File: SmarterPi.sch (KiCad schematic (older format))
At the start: 19 parts, among them J1 Raspberry_Pi_2_3, J2 RJ10, J3 Screw_Terminal_01x04, J4 Screw_Terminal_01x03, J5 Screw_Terminal_01x04, SW1 SW_Push, SW2 SW_Push, SW3 SW_Push

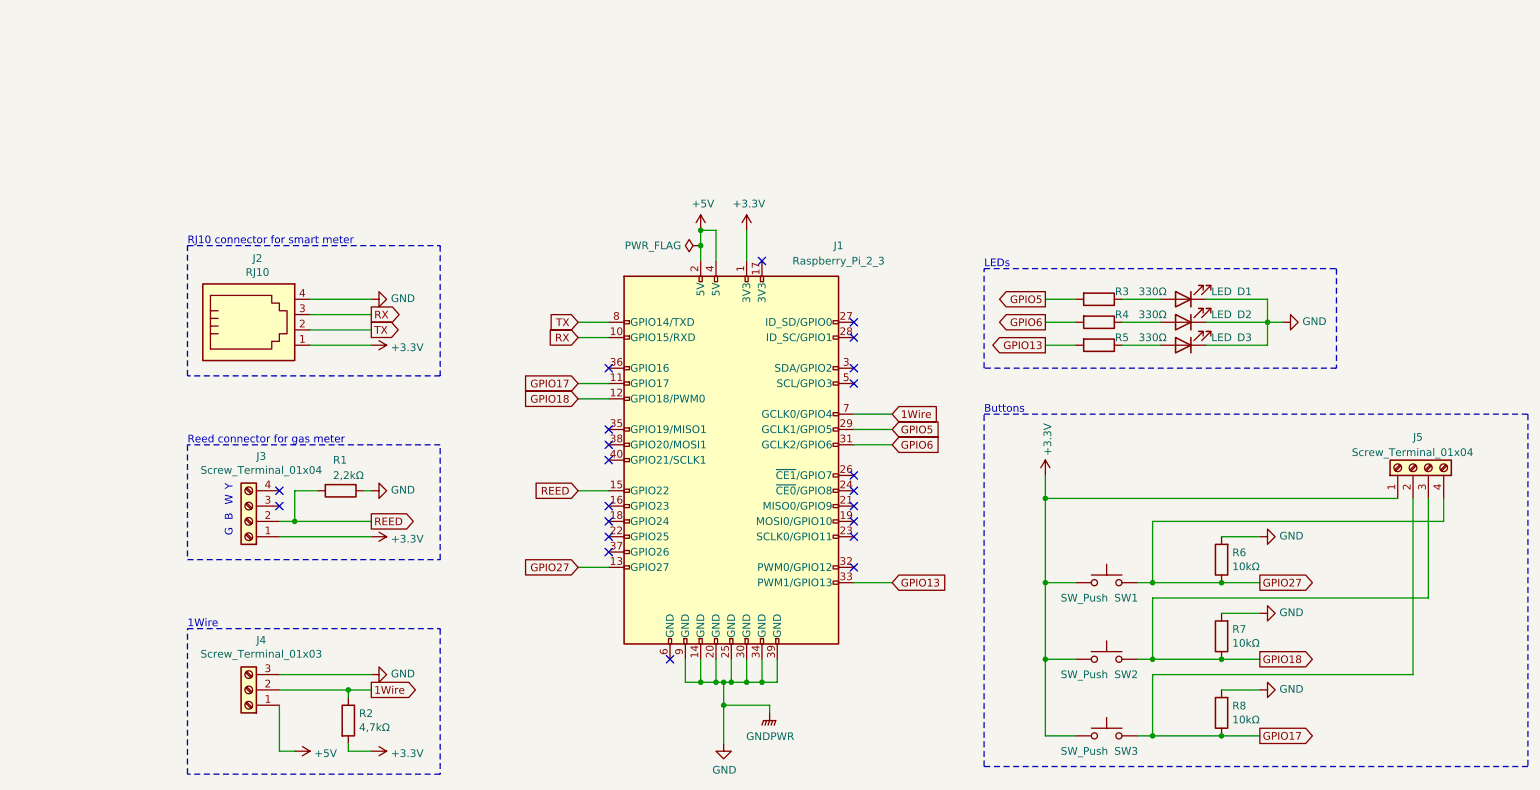
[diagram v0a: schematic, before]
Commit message: Added DS18B20
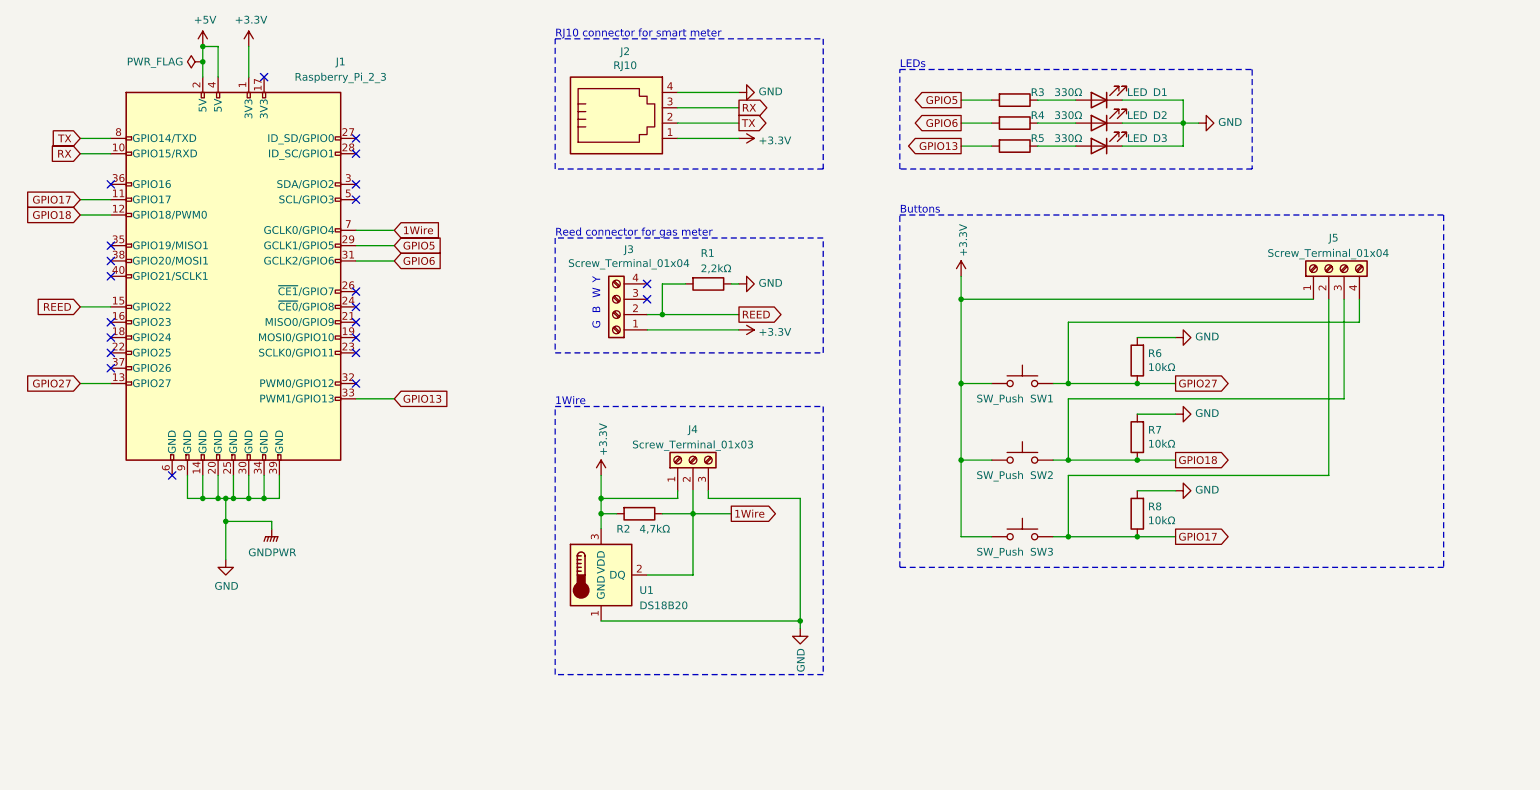
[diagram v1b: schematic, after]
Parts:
- added U1: DS18B20, Package_TO_SOT_THT:TO-92_Inline, symbol Sensor_Temperature:DS18B20
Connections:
- net +3V3: now also J4.1 (Pin_1), U1.3 (VDD)
- net +5V: no longer J4.1 (Pin_1)
- net 1Wire: now also U1.2 (DQ)
- net GND: now also U1.1 (GND)
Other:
- moved on the sheet: D1, D2, D3, J1, J2, J3, J4, J5, R1, R2, R3, R4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
